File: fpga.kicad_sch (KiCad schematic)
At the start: 83 parts, among them P1 JTAG_CONN, P3 mSD_CONN, Q1 BC847, Q2 BC857, SW2 SW_PUSH, SW3 SW_PUSH, U10 S25FL216K, U11 IRM-V538/TR1, U2 EP4CE15E22

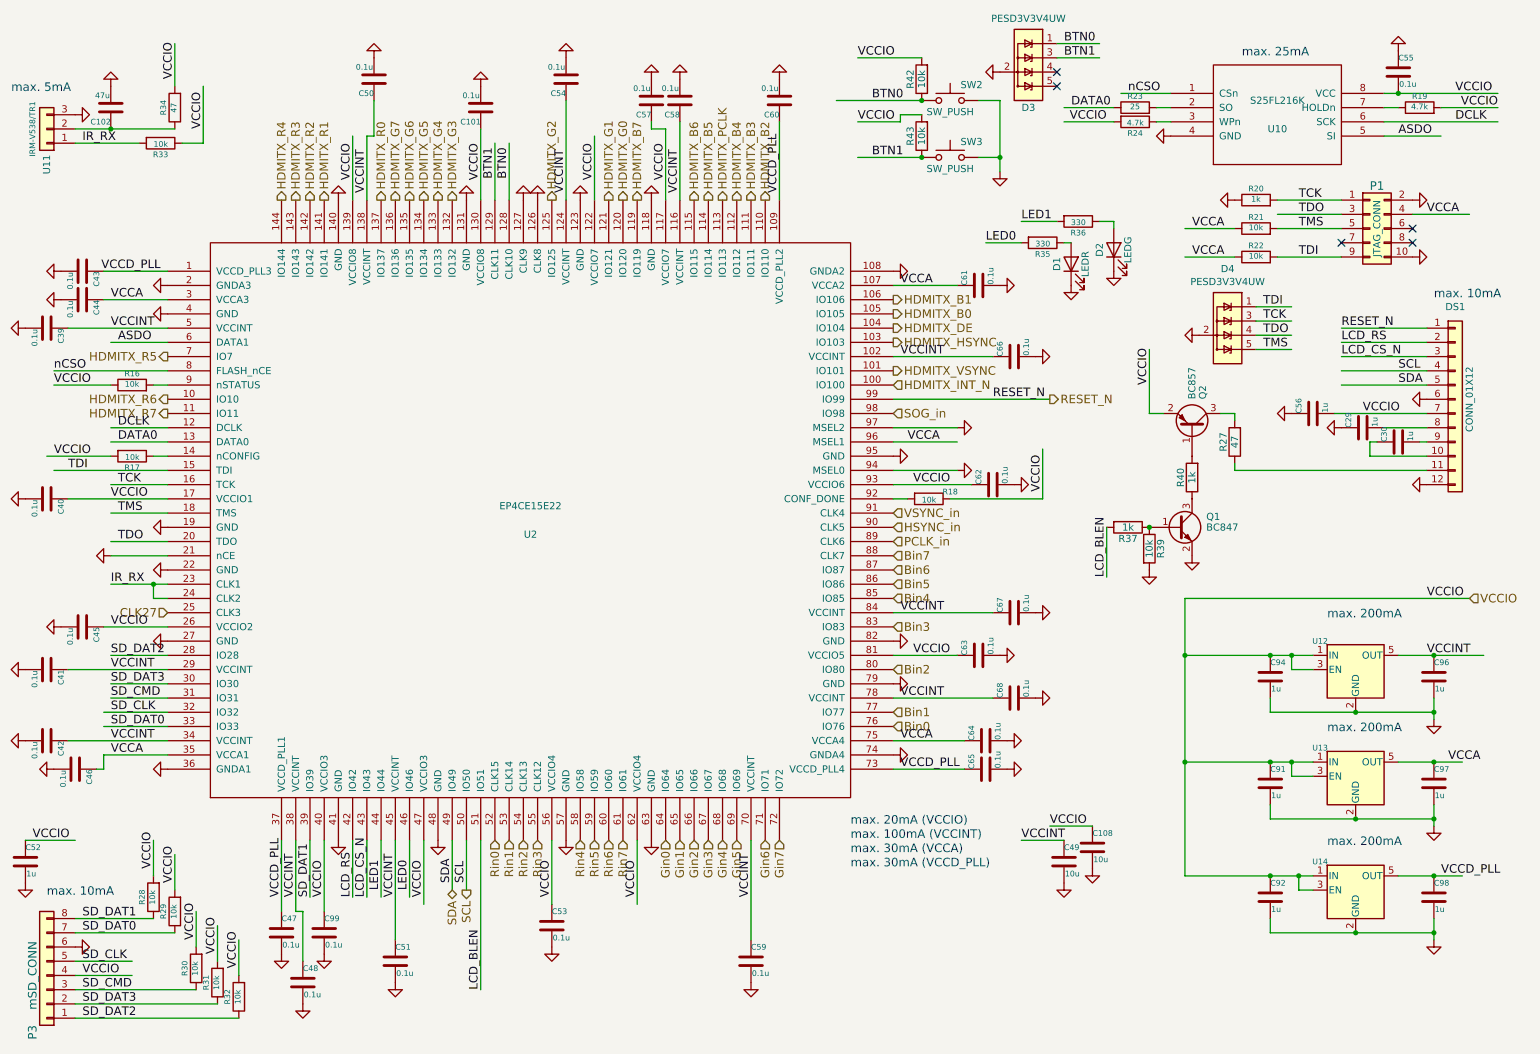
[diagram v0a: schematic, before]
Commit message: additional updates for PCB v1.8
* change to 4-layer stackup for better power delivery
* choose another FPGA pin for PCB version indicator
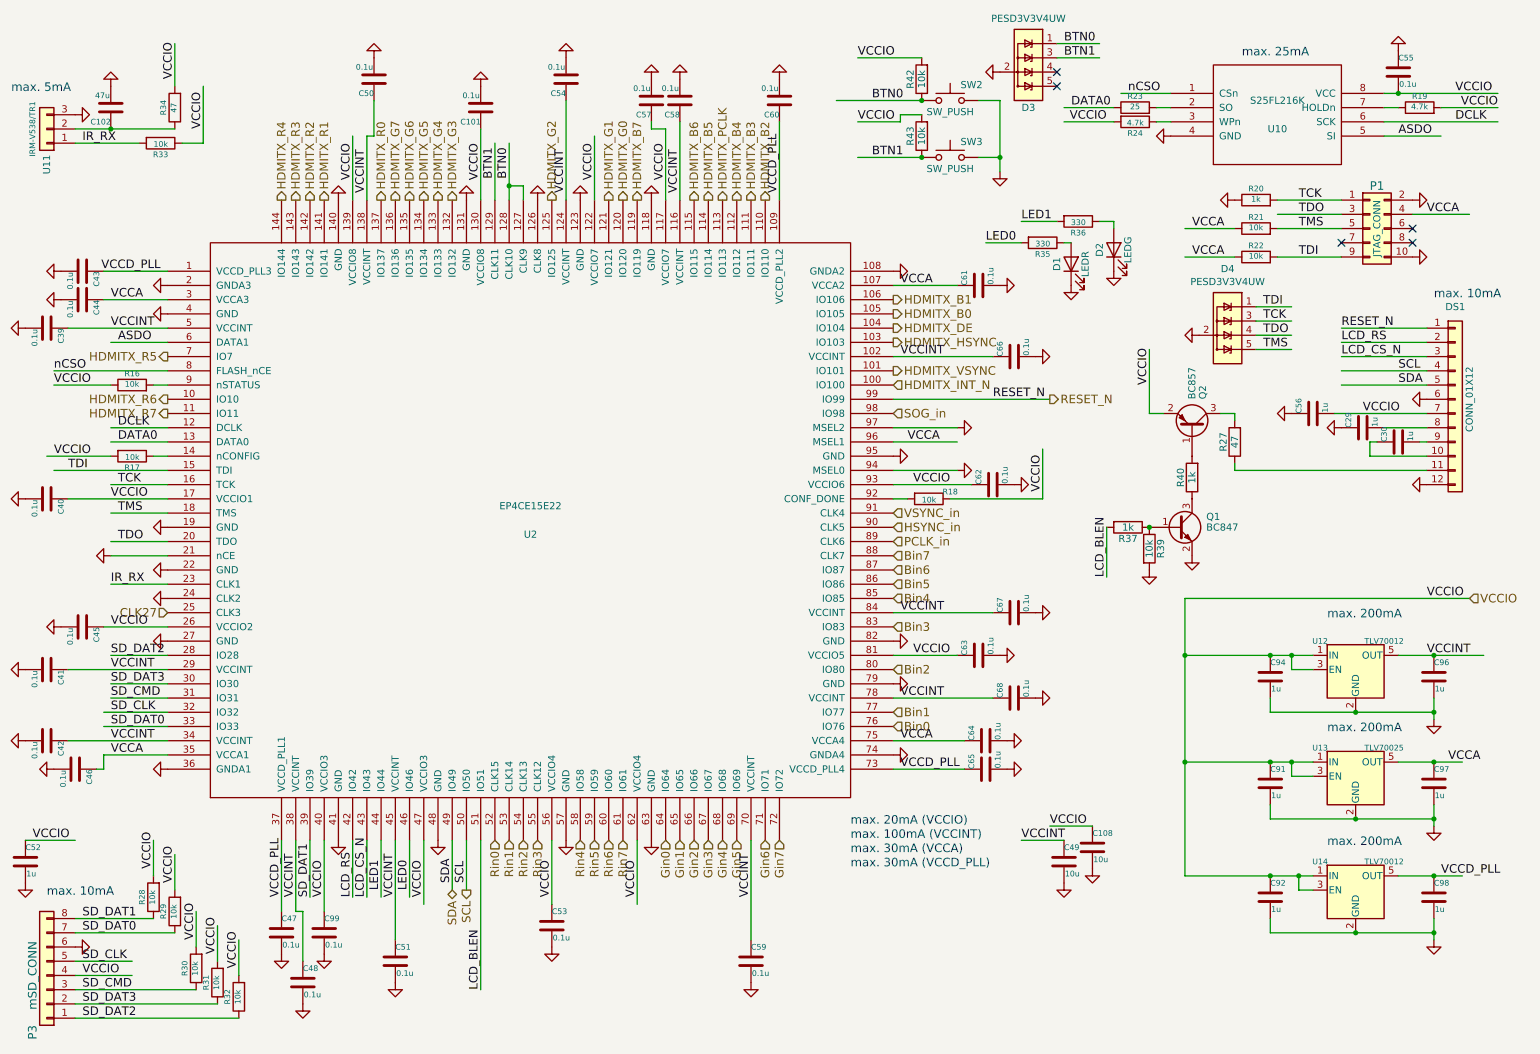
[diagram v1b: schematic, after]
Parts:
- U12, U14: value (none) -> TLV70012; footprint (none) -> custom_components:SOT-23-5_Handsoldering
- U13: value (none) -> TLV70025; footprint (none) -> custom_components:SOT-23-5_Handsoldering
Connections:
- net BTN0: now also U2.127 (CLK9)
- net GND: now also U2.24 (CLK2); no longer U2.127 (CLK9)
- net IR_RX: no longer U2.24 (CLK2)
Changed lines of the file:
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@@
     (rev "1.8")
   )
-  (junction (at 40.64 115.57) (diameter 0) (color 0 0 0 0)
-  )
   (junction (at 269.24 147.32) (diameter 0) (color 0 0 0 0)
   )
@@
   (junction (at 177.8 29.21) (diameter 0) (color 0 0 0 0)
   )
+  (junction (at 104.14 44.45) (diameter 0) (color 0 0 0 0)
+  )
   (junction (at 191.77 39.37) (diameter 0) (color 0 0 0 0)
   )
@@
     (stroke (width 0) (type default) (color 0 0 0 0))
   )
+  (wire (pts (xy 104.14 44.45) (xy 106.68 44.45))
+    (stroke (width 0) (type default) (color 0 0 0 0))
+  )
   (wire (pts (xy 218.44 85.09) (xy 220.98 85.09))
     (stroke (width 0) (type default) (color 0 0 0 0))
@@
     (stroke (width 0) (type default) (color 0 0 0 0))
   )
-  (wire (pts (xy 40.64 118.11) (xy 40.64 115.57))
-    (stroke (width 0) (type default) (color 0 0 0 0))
-  )
   (wire (pts (xy 243.84 128.27) (xy 243.84 130.81))
     (stroke (width 0) (type default) (color 0 0 0 0))
@@
     (stroke (width 0) (type default) (color 0 0 0 0))
   )
+  (wire (pts (xy 104.14 44.45) (xy 104.14 36.83))
+    (stroke (width 0) (type default) (color 0 0 0 0))
+  )
   (wire (pts (xy 80.01 29.21) (xy 80.01 35.56))
     (stroke (width 0) (type default) (color 0 0 0 0))
@@
     (stroke (width 0) (type default) (color 0 0 0 0))
   )
-  (wire (pts (xy 104.14 46.99) (xy 104.14 36.83))
+  (wire (pts (xy 104.14 46.99) (xy 104.14 44.45))
     (stroke (width 0) (type default) (color 0 0 0 0))
   )
@@
     (stroke (width 0) (type default) (color 0 0 0 0))
   )
-  (wire (pts (xy 40.64 115.57) (xy 43.18 115.57))
+  (wire (pts (xy 33.02 115.57) (xy 43.18 115.57))
     (stroke (width 0) (type default) (color 0 0 0 0))
   )
@@
     (stroke (width 0) (type default) (color 0 0 0 0))
   )
-  (wire (pts (xy 43.18 118.11) (xy 40.64 118.11))
-    (stroke (width 0) (type default) (color 0 0 0 0))
-  )
   (wire (pts (xy 166.37 39.37) (xy 177.8 39.37))
     (stroke (width 0) (type default) (color 0 0 0 0))
@@
     (stroke (width 0) (type default) (color 0 0 0 0))
   )
+  (wire (pts (xy 106.68 44.45) (xy 106.68 46.99))
+    (stroke (width 0) (type default) (color 0 0 0 0))
+  )
   (wire (pts (xy 33.02 110.49) (xy 43.18 110.49))
     (stroke (width 0) (type default) (color 0 0 0 0))
@@
     (stroke (width 0) (type default) (color 0 0 0 0))
   )
-  (wire (pts (xy 33.02 115.57) (xy 40.64 115.57))
-    (stroke (width 0) (type default) (color 0 0 0 0))
-  )
   (wire (pts (xy 43.18 128.27) (xy 33.02 128.27))
     (stroke (width 0) (type default) (color 0 0 0 0))
@@
       (effects (font (size 1.016 1.016)))
     )
-    (property "Value" "" (id 1) (at 260.35 165.1 0)
+    (property "Value" "TLV70012" (id 1) (at 260.35 165.1 0)
       (effects (font (size 1.016 1.016)))
     )
-    (property "Footprint" "" (id 2) (at 255.27 167.64 0)
+    (property "Footprint" "custom_components:SOT-23-5_Handsoldering" (id 2) (at 255.27 167.64 0)
       (effects (font (size 0.889 0.889) italic) hide)
     )
@@
       (effects (font (size 1.016 1.016)))
     )
-    (property "Value" "" (id 1) (at 260.35 144.78 0)
+    (property "Value" "TLV70025" (id 1) (at 260.35 144.78 0)
       (effects (font (size 1.016 1.016)))
     )
-    (property "Footprint" "" (id 2) (at 255.27 147.32 0)
+    (property "Footprint" "custom_components:SOT-23-5_Handsoldering" (id 2) (at 255.27 147.32 0)
       (effects (font (size 0.889 0.889) italic) hide)
     )
@@
       (effects (font (size 1.016 1.016)))
     )
-    (property "Value" "" (id 1) (at 260.35 125.73 0)
+    (property "Value" "TLV70012" (id 1) (at 260.35 125.73 0)
       (effects (font (size 1.016 1.016)))
     )
-    (property "Footprint" "" (id 2) (at 255.27 128.27 0)
+    (property "Footprint" "custom_components:SOT-23-5_Handsoldering" (id 2) (at 255.27 128.27 0)
       (effects (font (size 0.889 0.889) italic) hide)
     )
@@
     (pin "8")
   )
-  (symbol (lib_id "power:GND") (at 106.68 46.99 180) (unit 1)
-    (in_bom yes) (on_board yes)
-    (property "Reference" "#PWR065" (id 0) (at 106.68 46.99 0)
-      (effects (font (size 0.762 0.762)) hide)
-    )
-    (property "Value" "GND" (id 1) (at 106.68 45.212 0)
-      (effects (font (size 0.762 0.762)) hide)
-    )
-    (property "Footprint" "" (id 2) (at 106.68 46.99 0)
-      (effects (font (size 1.524 1.524)) hide)
-    )
-    (property "Datasheet" "" (id 3) (at 106.68 46.99 0)
-      (effects (font (size 1.524 1.524)))
-    )
-    (pin "1")
-  )
   (symbol (lib_id "power:GND") (at 109.22 46.99 180) (unit 1)
     (in_bom yes) (on_board yes)
@@
       (effects (font (size 1.524 1.524)))
     )
+    (pin "1")
+  )
+  (symbol (lib_id "power:GND") (at 43.18 118.11 270) (unit 1)
+    (in_bom yes) (on_board yes)
+    (property "Reference" "#PWR0131" (id 0) (at 43.18 118.11 0)
+      (effects (font (size 0.762 0.762)) hide)
+    )
+    (property "Value" "GND" (id 1) (at 41.402 118.11 0)
+      (effects (font (size 0.762 0.762)) hide)
+    )
+    (property "Footprint" "" (id 2) (at 43.18 118.11 0)
+      (effects (font (size 1.524 1.524)) hide)
+    )
+    (property "Datasheet" "" (id 3) (at 43.18 118.11 0)
+      (effects (font (size 1.524 1.524)))
+    )
